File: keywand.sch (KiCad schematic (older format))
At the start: 25 parts

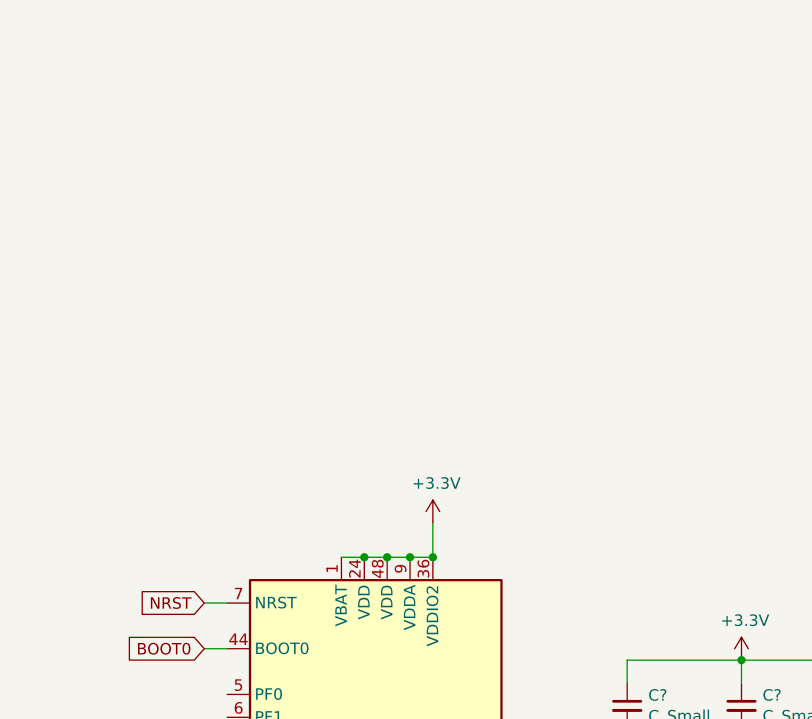
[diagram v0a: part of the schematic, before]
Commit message: Now with more usb-c!
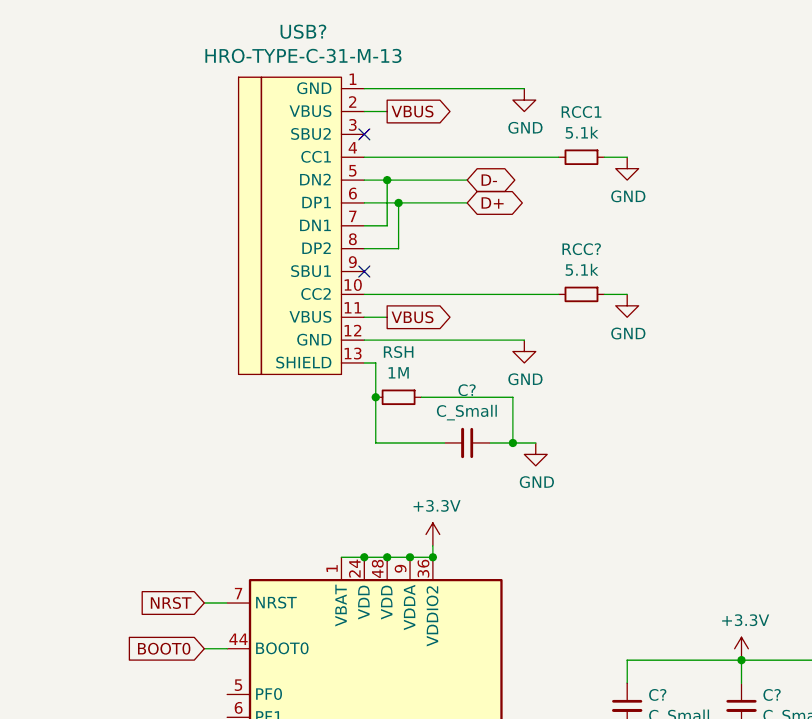
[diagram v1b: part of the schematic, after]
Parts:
- added C?: C_Small, symbol Device:C_Small
- added RCC1, RCC?: 5.1k, Resistor_SMD:R_0805_2012Metric, symbol Device:R_Small
- added RSH: 1M, Resistor_SMD:R_0805_2012Metric, symbol Device:R_Small
- added USB?: HRO-TYPE-C-31-M-13, Type-C:HRO-TYPE-C-31-M-13, symbol Type-C:HRO-TYPE-C-31-M-12
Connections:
- net D+: now also USB?.6 (DP1), USB?.8 (DP2)
- net D-: now also USB?.5 (DN2), USB?.7 (DN1)
- net GND: now also C?.1, RCC1.1, RCC?.1, RSH.1, USB?.1 (GND), USB?.12 (GND)
- new net: RCC?.2, USB?.10 (CC2)
- new net: C?.2, RSH.2, USB?.13 (SHIELD)
- new net: RCC1.2, USB?.4 (CC1)
- new net VBUS: USB?.11 (VBUS), USB?.2 (VBUS)
- no-connect marks 0 -> 2
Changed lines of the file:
@@
 L power:+3.3V #PWR?
 U 1 1 5F002DB1
-P 7800 2800
-F 0 "#PWR?" H 7800 2650 50  0001 C CNN
-F 1 "+3.3V" H 7815 2973 50  0000 C CNN
-F 2 "" H 7800 2800 50  0001 C CNN
-F 3 "" H 7800 2800 50  0001 C CNN
-	1    7800 2800
-	1    0    0    -1
-$EndComp
-Wire Wire Line
-	7800 2800 7800 2950
+P 7800 2900
+F 0 "#PWR?" H 7800 2750 50  0001 C CNN
+F 1 "+3.3V" H 7815 3073 50  0000 C CNN
+F 2 "" H 7800 2900 50  0001 C CNN
+F 3 "" H 7800 2900 50  0001 C CNN
+	1    7800 2900
+	1    0    0    -1
+$EndComp
 Wire Wire Line
 	7800 2950 7700 2950
-Connection ~ 7800 2950
 Connection ~ 7500 2950
 Wire Wire Line
@@
 Wire Wire Line
 	3400 5650 3400 5700
+$Comp
+L Type-C:HRO-TYPE-C-31-M-12 USB?
+U 1 1 5F04F7D3
+P 7400 1450
+F 0 "USB?" H 7233 2247 60  0000 C CNN
+F 1 "HRO-TYPE-C-31-M-13" H 7233 2141 60  0000 C CNN
+F 2 "Type-C:HRO-TYPE-C-31-M-13" H 7400 1450 60  0001 C CNN
+F 3 "" H 7400 1450 60  0001 C CNN
+F 4 "C223906" H 7400 1450 50  0001 C CNN "LCSC"
+	1    7400 1450
+	1    0    0    -1
+$EndComp
+$Comp
+L power:GND #PWR?
+U 1 1 5F05243B
+P 8200 900
+F 0 "#PWR?" H 8200 650 50  0001 C CNN
+F 1 "GND" H 8205 727 50  0000 C CNN
+F 2 "" H 8200 900 50  0001 C CNN
+F 3 "" H 8200 900 50  0001 C CNN
+	1    8200 900
+	1    0    0    -1
+$EndComp
+Text GLabel 7600 1000 2    50   Output ~ 0
+VBUS
+Wire Wire Line
+	7600 1000 7500 1000
+Wire Wire Line
+	7500 900  8200 900
+$Comp
+L power:GND #PWR?
+U 1 1 5F0569C5
+P 8200 2000
+F 0 "#PWR?" H 8200 1750 50  0001 C CNN
+F 1 "GND" H 8205 1827 50  0000 C CNN
+F 2 "" H 8200 2000 50  0001 C CNN
+F 3 "" H 8200 2000 50  0001 C CNN
+	1    8200 2000
+	1    0    0    -1
+$EndComp
+Wire Wire Line
+	8200 2000 7500 2000
+Text GLabel 7600 1900 2    50   Output ~ 0
+VBUS
+Wire Wire Line
+	7600 1900 7500 1900
+$Comp
+L Device:R_Small RCC1
+U 1 1 5F05A565
+P 8450 1200
+F 0 "RCC1" V 8254 1200 50  0000 C CNN
+F 1 "5.1k" V 8345 1200 50  0000 C CNN
+F 2 "Resistor_SMD:R_0805_2012Metric" H 8450 1200 50  0001 C CNN
+F 3 "~" H 8450 1200 50  0001 C CNN
+F 4 "C27834" V 8450 1200 50  0001 C CNN "Field4"
+	1    8450 1200
+	0    1    1    0
+$EndComp
+Wire Wire Line
+	7500 1200 8350 1200
+Wire Wire Line
+	8550 1200 8650 1200
+$Comp
+L power:GND #PWR?
+U 1 1 5F05F303
+P 8650 1200
+F 0 "#PWR?" H 8650 950 50  0001 C CNN
+F 1 "GND" H 8655 1027 50  0000 C CNN
+F 2 "" H 8650 1200 50  0001 C CNN
+F 3 "" H 8650 1200 50  0001 C CNN
+	1    8650 1200
+	1    0    0    -1
+$EndComp
+$Comp
+L Device:R_Small RCC?
+U 1 1 5F060516
+P 8450 1800
+F 0 "RCC?" V 8254 1800 50  0000 C CNN
+F 1 "5.1k" V 8345 1800 50  0000 C CNN
+F 2 "Resistor_SMD:R_0805_2012Metric" H 8450 1800 50  0001 C CNN
+F 3 "~" H 8450 1800 50  0001 C CNN
+F 4 "C27834" V 8450 1800 50  0001 C CNN "Field4"
+	1    8450 1800
+	0    1    1    0
+$EndComp
+Wire Wire Line
+	7500 1800 8350 1800
+Wire Wire Line
+	8550 1800 8650 1800
+$Comp
+L power:GND #PWR?
+U 1 1 5F06051E
+P 8650 1800
+F 0 "#PWR?" H 8650 1550 50  0001 C CNN
+F 1 "GND" H 8655 1627 50  0000 C CNN
+F 2 "" H 8650 1800 50  0001 C CNN
+F 3 "" H 8650 1800 50  0001 C CNN
+	1    8650 1800
+	1    0    0    -1
+$EndComp
+Text GLabel 7950 1300 2    50   BiDi ~ 0
+D-
+Text GLabel 7950 1400 2    50   BiDi ~ 0
+D+
+Wire Wire Line
+	7950 1300 7600 1300
+Wire Wire Line
+	7500 1400 7650 1400
+Wire Wire Line
+	7500 1600 7650 1600
+Wire Wire Line
+	7650 1600 7650 1400
+Connection ~ 7650 1400
+Wire Wire Line
+	7650 1400 7950 1400
+Wire Wire Line
+	7500 1500 7600 1500
+Wire Wire Line
+	7600 1500 7600 1300
+Connection ~ 7600 1300
+Wire Wire Line
+	7600 1300 7500 1300
+$Comp
+L Device:R_Small RSH
+U 1 1 5F06A9A0
+P 7650 2250
+F 0 "RSH" V 7454 2250 50  0000 C CNN
+F 1 "1M" V 7545 2250 50  0000 C CNN
+F 2 "Resistor_SMD:R_0805_2012Metric" H 7650 2250 50  0001 C CNN
+F 3 "~" H 7650 2250 50  0001 C CNN
+F 4 "C17514" V 7650 2250 50  0001 C CNN "Field4"
+	1    7650 2250
+	0    1    1    0
+$EndComp
+$Comp
+L Device:C_Small C?
+U 1 1 5F06B0CC
+P 7950 2450
+F 0 "C?" V 7721 2450 50  0000 C CNN
+F 1 "C_Small" V 7812 2450 50  0000 C CNN
+F 2 "" H 7950 2450 50  0001 C CNN
+F 3 "~" H 7950 2450 50  0001 C CNN
+	1    7950 2450
+	0    1    1    0
+$EndComp
+Wire Wire Line
+	7500 2100 7550 2100
+Wire Wire Line
+	7550 2100 7550 2250
+Wire Wire Line
+	7550 2450 7850 2450
+Connection ~ 7550 2250
+Wire Wire Line
+	7750 2250 8150 2250
+Wire Wire Line
+	8150 2450 8050 2450
+$Comp
+L power:GND #PWR?
+U 1 1 5F070EE9
+P 8250 2450
+F 0 "#PWR?" H 8250 2200 50  0001 C CNN
+F 1 "GND" H 8255 2277 50  0000 C CNN
+F 2 "" H 8250 2450 50  0001 C CNN
+F 3 "" H 8250 2450 50  0001 C CNN
+	1    8250 2450
+	1    0    0    -1
+$EndComp
+Wire Wire Line
+	8250 2450 8150 2450
+Connection ~ 8150 2450
+NoConn ~ 7500 1100
+NoConn ~ 7500 1700
+Wire Wire Line
+	7800 2900 7800 2950
+Connection ~ 7800 2950
+Wire Wire Line
+	8150 2250 8150 2450
+Wire Wire Line
+	7550 2250 7550 2450
 $EndSCHEMATC

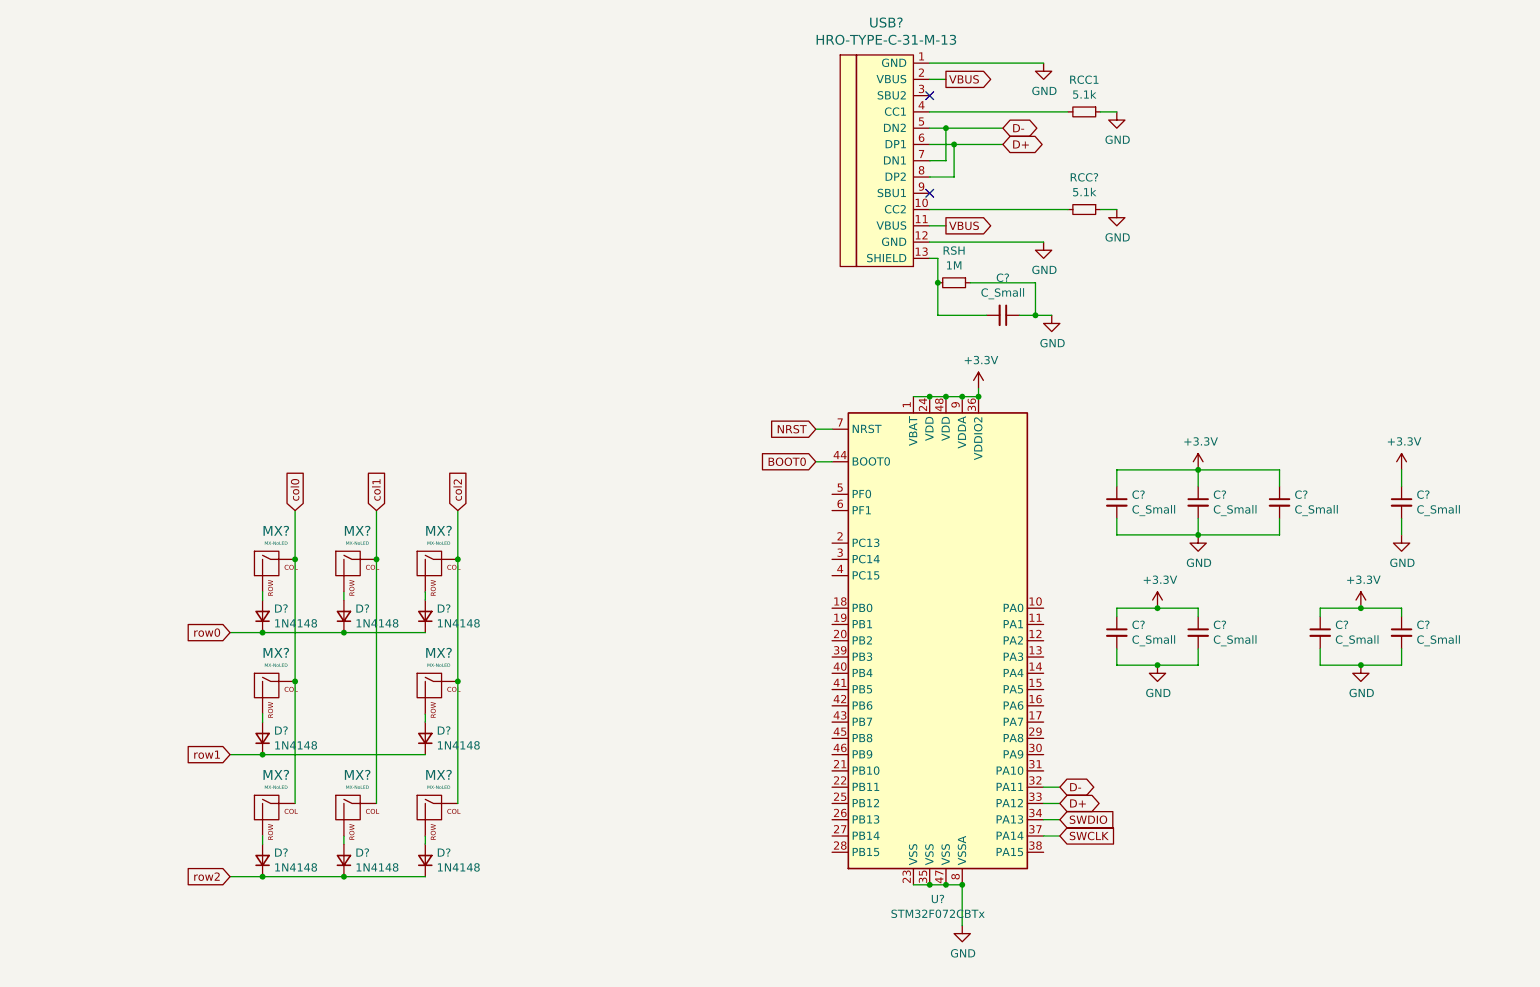
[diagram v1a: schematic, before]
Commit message: Updated layout just so it's a little easier to parse. more boxes to come
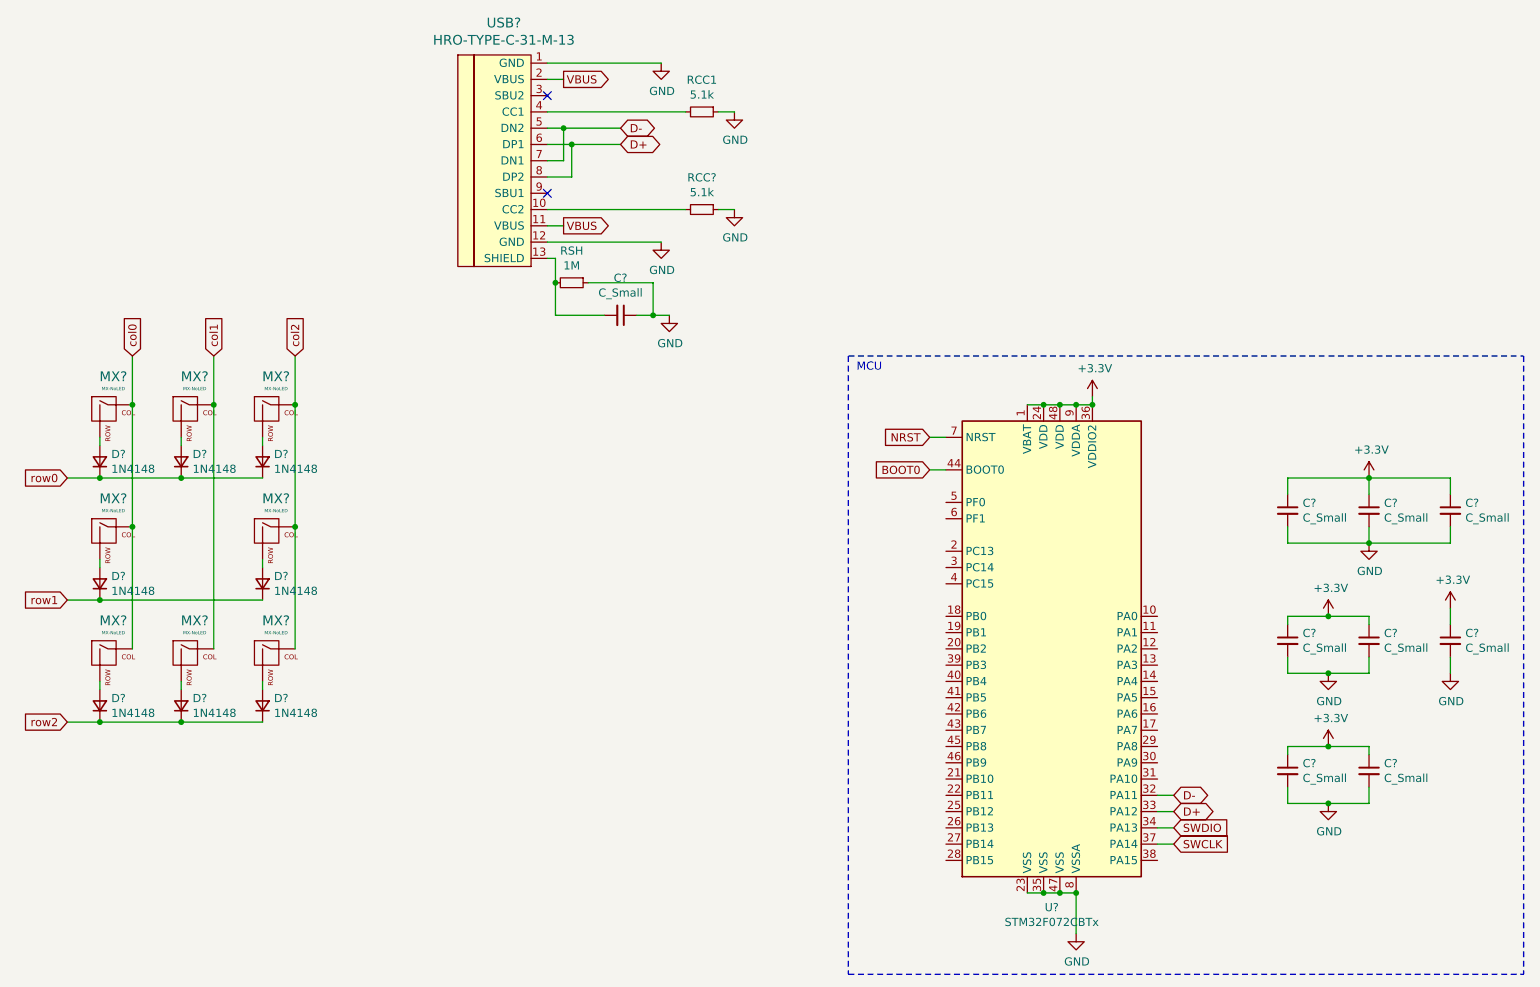
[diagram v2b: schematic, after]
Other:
- note added: "MCU"
- moved on the sheet: C?, D?, MX?, RCC1, RCC?, RSH, U?, USB?
